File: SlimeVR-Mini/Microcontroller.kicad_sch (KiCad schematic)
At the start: 8 parts, among them U1 ESP32-C3-MINI-1-N4

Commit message: IMU wiring done-ish
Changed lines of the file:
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@@
     (effects (font (size 1.27 1.27)) (justify left bottom))
+  )
+  (hierarchical_label "SDA" (shape input) (at 181.61 105.41 0) (fields_autoplaced)
+    (effects (font (size 1.27 1.27)) (justify left))
+  )
+  (hierarchical_label "SCL" (shape input) (at 181.61 107.95 0) (fields_autoplaced)
+    (effects (font (size 1.27 1.27)) (justify left))
   )
   (symbol (lib_id "power:GND") (at 106.68 111.76 0) (unit 1)

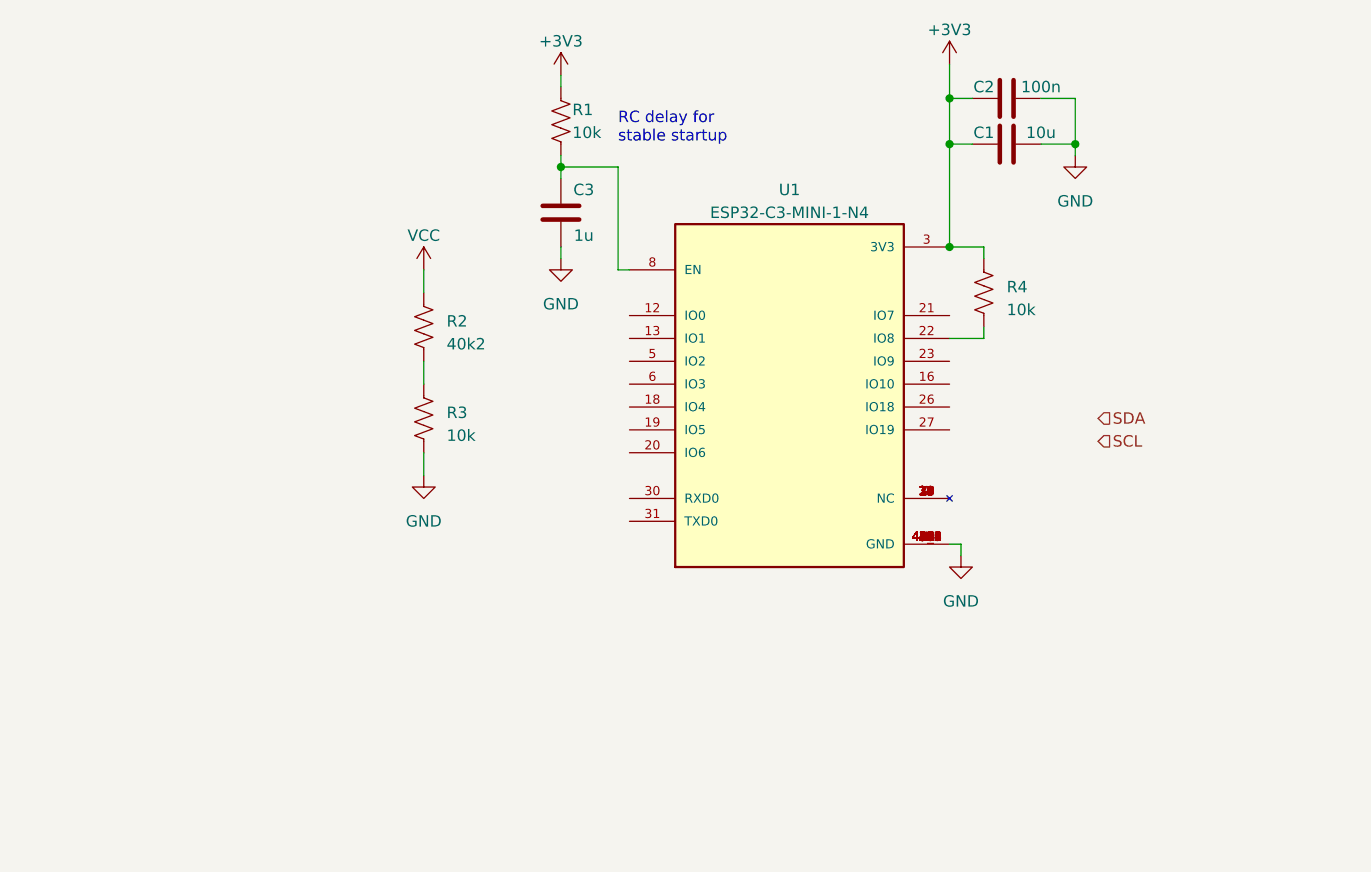
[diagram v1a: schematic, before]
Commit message: added Power page + fixing symbols and footprints
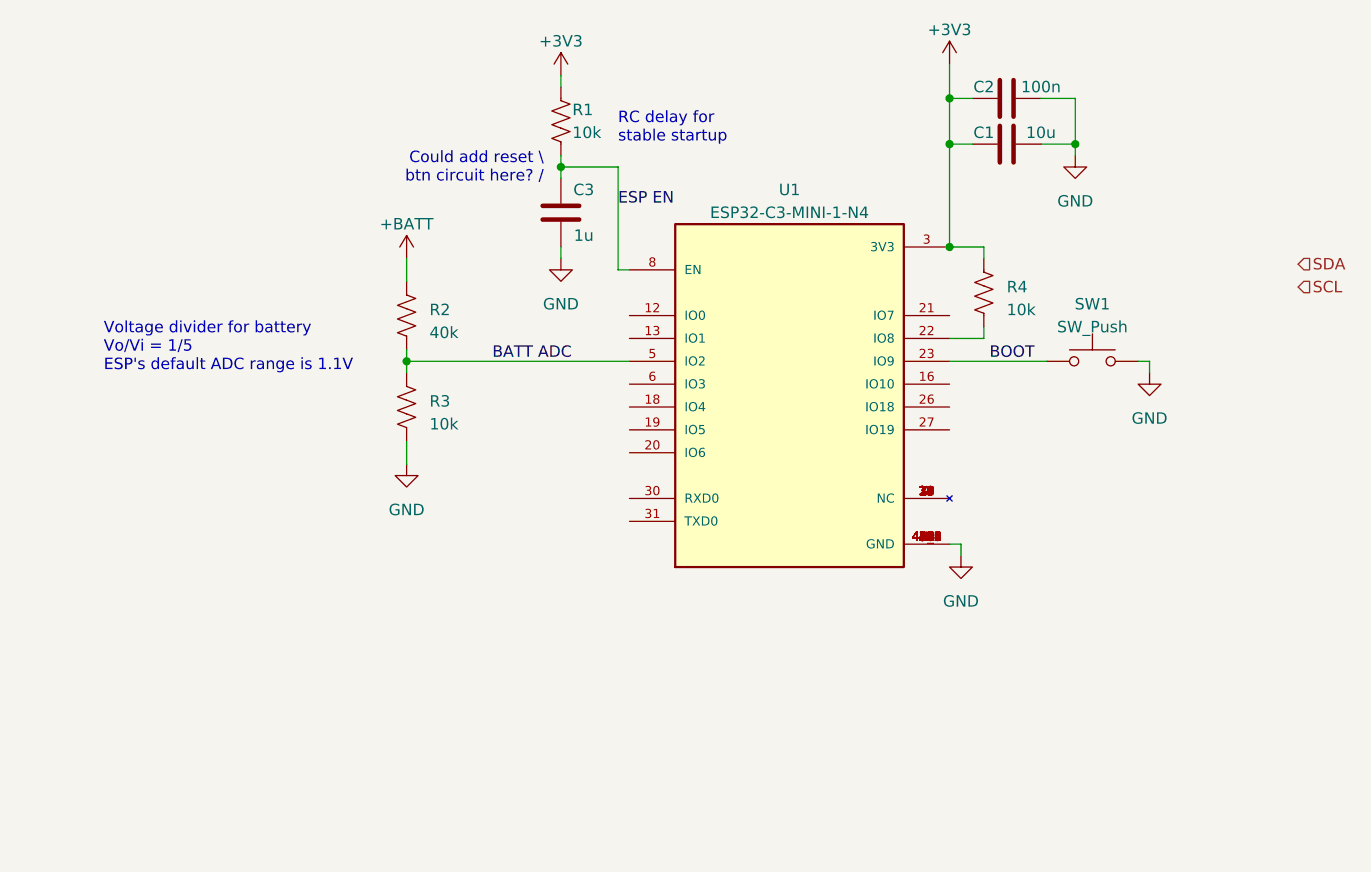
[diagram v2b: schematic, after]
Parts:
- added SW1: SW_Push, symbol Switch:SW_Push
- R2: value 40k2 -> 40k
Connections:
- net GND: now also SW1.2
- net ESP EN: now reaches C3.1, R1.2, U1.8 (EN)
- net BOOT: now reaches U1.23 (IO9)
- net BOOT: now also SW1.1
- net BATT ADC: now reaches U1.5 (IO2)
- net BATT ADC: now also R2.2, R3.1
- net VCC renamed +BATT
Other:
- note added: "Could add reset \ btn circuit here? /"
- note added: "Voltage divider for battery Vo/Vi = 1/5 ESP's default ADC range is 1.1V"
- moved on the sheet: R2, R3
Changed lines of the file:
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@@
   (junction (at 165.1 86.36) (diameter 0) (color 0 0 0 0)
   )
+  (junction (at 104.775 99.06) (diameter 0) (color 0 0 0 0)
+  )
   (junction (at 165.1 69.85) (diameter 0) (color 0 0 0 0)
   )
@@
     (stroke (width 0) (type default))
   )
+  (wire (pts (xy 104.775 99.06) (xy 104.775 100.33))
+    (stroke (width 0) (type default))
+  )
+  (wire (pts (xy 187.325 99.06) (xy 187.325 100.33))
+    (stroke (width 0) (type default))
+  )
   (wire (pts (xy 179.07 69.85) (xy 179.07 74.93))
     (stroke (width 0) (type default))
@@
     (stroke (width 0) (type default))
   )
-  (wire (pts (xy 106.68 88.9) (xy 106.68 91.44))
-    (stroke (width 0) (type default))
-  )
-  (wire (pts (xy 106.68 99.06) (xy 106.68 101.6))
+  (wire (pts (xy 104.775 87.63) (xy 104.775 90.17))
+    (stroke (width 0) (type default))
+  )
+  (wire (pts (xy 104.775 97.79) (xy 104.775 99.06))
     (stroke (width 0) (type default))
   )
@@
     (stroke (width 0) (type default))
   )
-  (wire (pts (xy 106.68 109.22) (xy 106.68 111.76))
+  (wire (pts (xy 104.775 107.95) (xy 104.775 110.49))
+    (stroke (width 0) (type default))
+  )
+  (wire (pts (xy 186.055 99.06) (xy 187.325 99.06))
     (stroke (width 0) (type default))
   )
@@
     (stroke (width 0) (type default))
   )
+  (wire (pts (xy 104.775 99.06) (xy 129.54 99.06))
+    (stroke (width 0) (type default))
+  )
   (wire (pts (xy 165.1 119.38) (xy 166.37 119.38))
     (stroke (width 0) (type default))
   )
+  (wire (pts (xy 165.1 99.06) (xy 175.895 99.06))
+    (stroke (width 0) (type default))
+  )
   (wire (pts (xy 165.1 66.04) (xy 165.1 69.85))
     (stroke (width 0) (type default))
@@
   (wire (pts (xy 121.92 67.31) (xy 121.92 68.58))
     (stroke (width 0) (type default))
+  )
+  (text "Voltage divider for battery\nVo/Vi = 1/5\nESP's default ADC range is 1.1V"
+    (at 71.12 100.33 0)
+    (effects (font (size 1.27 1.27)) (justify left bottom))
   )
   (text "RC delay for\nstable startup" (at 128.27 74.93 0)
     (effects (font (size 1.27 1.27)) (justify left bottom))
   )
-  (hierarchical_label "SDA" (shape input) (at 181.61 105.41 0) (fields_autoplaced)
+  (text "Could add reset \\\nbtn circuit here? /" (at 120.015 79.375 0)
+    (effects (font (size 1.27 1.27)) (justify right bottom))
+  )
+  (label "BOOT" (at 169.545 99.06 0) (fields_autoplaced)
+    (effects (font (size 1.27 1.27)) (justify left bottom))
+  )
+  (label "BATT ADC" (at 114.3 99.06 0) (fields_autoplaced)
+    (effects (font (size 1.27 1.27)) (justify left bottom))
+  )
+  (label "ESP EN" (at 128.27 81.915 0) (fields_autoplaced)
+    (effects (font (size 1.27 1.27)) (justify left bottom))
+  )
+  (hierarchical_label "SDA" (shape input) (at 203.835 88.265 0) (fields_autoplaced)
     (effects (font (size 1.27 1.27)) (justify left))
   )
-  (hierarchical_label "SCL" (shape input) (at 181.61 107.95 0) (fields_autoplaced)
+  (hierarchical_label "SCL" (shape input) (at 203.835 90.805 0) (fields_autoplaced)
     (effects (font (size 1.27 1.27)) (justify left))
   )
-  (symbol (lib_id "power:GND") (at 106.68 111.76 0) (unit 1)
-    (in_bom yes) (on_board yes) (dnp no) (fields_autoplaced)
-    (property "Reference" "#PWR03" (at 106.68 118.11 0)
-      (effects (font (size 1.27 1.27)) hide)
-    )
-    (property "Value" "GND" (at 106.68 116.84 0)
-      (effects (font (size 1.27 1.27)))
-    )
-    (property "Footprint" "" (at 106.68 111.76 0)
-      (effects (font (size 1.27 1.27)) hide)
-    )
-    (property "Datasheet" "" (at 106.68 111.76 0)
+  (symbol (lib_id "power:GND") (at 187.325 100.33 0) (unit 1)
+    (in_bom yes) (on_board yes) (dnp no) (fields_autoplaced)
+    (property "Reference" "#PWR04" (at 187.325 106.68 0)
+      (effects (font (size 1.27 1.27)) hide)
+    )
+    (property "Value" "GND" (at 187.325 105.41 0)
+      (effects (font (size 1.27 1.27)))
+    )
+    (property "Footprint" "" (at 187.325 100.33 0)
+      (effects (font (size 1.27 1.27)) hide)
+    )
+    (property "Datasheet" "" (at 187.325 100.33 0)
+      (effects (font (size 1.27 1.27)) hide)
+    )
+    (pin "1")
+    (instances
+      (project "SlimeVR-Mini"
+        (path "/01f70e2f-47c6-495b-b6f7-eee456c9fb57"
+          (reference "#PWR04") (unit 1)
+        )
+        (path "/01f70e2f-47c6-495b-b6f7-eee456c9fb57/35e02d93-cdac-48f7-b47e-4a5ff7382a35"
+          (reference "#PWR012") (unit 1)
+        )
+      )
+    )
+  )
+  (symbol (lib_id "power:GND") (at 104.775 110.49 0) (unit 1)
+    (in_bom yes) (on_board yes) (dnp no) (fields_autoplaced)
+    (property "Reference" "#PWR03" (at 104.775 116.84 0)
+      (effects (font (size 1.27 1.27)) hide)
+    )
+    (property "Value" "GND" (at 104.775 115.57 0)
+      (effects (font (size 1.27 1.27)))
+    )
+    (property "Footprint" "" (at 104.775 110.49 0)
+      (effects (font (size 1.27 1.27)) hide)
+    )
+    (property "Datasheet" "" (at 104.775 110.49 0)
       (effects (font (size 1.27 1.27)) hide)
     )
@@
         (path "/01f70e2f-47c6-495b-b6f7-eee456c9fb57/35e02d93-cdac-48f7-b47e-4a5ff7382a35"
           (reference "#PWR03") (unit 1)
+        )
+      )
+    )
+  )
+  (symbol (lib_id "power:+BATT") (at 104.775 87.63 0) (unit 1)
+    (in_bom yes) (on_board yes) (dnp no) (fields_autoplaced)
+    (property "Reference" "#PWR011" (at 104.775 91.44 0)
+      (effects (font (size 1.27 1.27)) hide)
+    )
+    (property "Value" "+BATT" (at 104.775 83.82 0)
+      (effects (font (size 1.27 1.27)))
+    )
+    (property "Footprint" "" (at 104.775 87.63 0)
+      (effects (font (size 1.27 1.27)) hide)
+    )
+    (property "Datasheet" "" (at 104.775 87.63 0)
+      (effects (font (size 1.27 1.27)) hide)
+    )
+    (pin "1")
+    (instances
+      (project "SlimeVR-Mini"
+        (path "/01f70e2f-47c6-495b-b6f7-eee456c9fb57/35e02d93-cdac-48f7-b47e-4a5ff7382a35"
+          (reference "#PWR011") (unit 1)
         )
       )
@@
     )
   )
-  (symbol (lib_id "Device:R_US") (at 106.68 95.25 0) (unit 1)
-    (in_bom yes) (on_board yes) (dnp no) (fields_autoplaced)
-    (property "Reference" "R2" (at 109.22 94.615 0)
-      (effects (font (size 1.27 1.27)) (justify left))
-    )
-    (property "Value" "40k2" (at 109.22 97.155 0)
-      (effects (font (size 1.27 1.27)) (justify left))
-    )
-    (property "Footprint" "" (at 107.696 95.504 90)
-      (effects (font (size 1.27 1.27)) hide)
-    )
-    (property "Datasheet" "~" (at 106.68 95.25 0)
+  (symbol (lib_id "Device:R_US") (at 104.775 93.98 0) (unit 1)
+    (in_bom yes) (on_board yes) (dnp no) (fields_autoplaced)
+    (property "Reference" "R2" (at 107.315 93.345 0)
+      (effects (font (size 1.27 1.27)) (justify left))
+    )
+    (property "Value" "40k" (at 107.315 95.885 0)
+      (effects (font (size 1.27 1.27)) (justify left))
+    )
+    (property "Footprint" "" (at 105.791 94.234 90)
+      (effects (font (size 1.27 1.27)) hide)
+    )
+    (property "Datasheet" "~" (at 104.775 93.98 0)
       (effects (font (size 1.27 1.27)) hide)
     )
@@
     )
   )
-  (symbol (lib_id "Device:R_US") (at 106.68 105.41 0) (unit 1)
-    (in_bom yes) (on_board yes) (dnp no) (fields_autoplaced)
-    (property "Reference" "R3" (at 109.22 104.775 0)
-      (effects (font (size 1.27 1.27)) (justify left))
-    )
-    (property "Value" "10k" (at 109.22 107.315 0)
-      (effects (font (size 1.27 1.27)) (justify left))
-    )
-    (property "Footprint" "" (at 107.696 105.664 90)
-      (effects (font (size 1.27 1.27)) hide)
-    )
-    (property "Datasheet" "~" (at 106.68 105.41 0)
+  (symbol (lib_id "Device:R_US") (at 104.775 104.14 0) (unit 1)
+    (in_bom yes) (on_board yes) (dnp no) (fields_autoplaced)
+    (property "Reference" "R3" (at 107.315 103.505 0)
+      (effects (font (size 1.27 1.27)) (justify left))
+    )
+    (property "Value" "10k" (at 107.315 106.045 0)
+      (effects (font (size 1.27 1.27)) (justify left))
+    )
+    (property "Footprint" "" (at 105.791 104.394 90)
+      (effects (font (size 1.27 1.27)) hide)
+    )
+    (property "Datasheet" "~" (at 104.775 104.14 0)
       (effects (font (size 1.27 1.27)) hide)
     )
@@
     )
   )
-  (symbol (lib_id "power:VCC") (at 106.68 88.9 0) (unit 1)
-    (in_bom yes) (on_board yes) (dnp no) (fields_autoplaced)
-    (property "Reference" "#PWR02" (at 106.68 92.71 0)
-      (effects (font (size 1.27 1.27)) hide)
-    )
-    (property "Value" "VCC" (at 106.68 85.09 0)
-      (effects (font (size 1.27 1.27)))
-    )
-    (property "Footprint" "" (at 106.68 88.9 0)
-      (effects (font (size 1.27 1.27)) hide)
-    )
-    (property "Datasheet" "" (at 106.68 88.9 0)
-      (effects (font (size 1.27 1.27)) hide)
-    )
-    (pin "1")
-    (instances
-      (project "SlimeVR-Mini"
-        (path "/01f70e2f-47c6-495b-b6f7-eee456c9fb57"
-          (reference "#PWR02") (unit 1)
-        )
-        (path "/01f70e2f-47c6-495b-b6f7-eee456c9fb57/35e02d93-cdac-48f7-b47e-4a5ff7382a35"
-          (reference "#PWR02") (unit 1)
-        )
-      )
-    )
-  )
   (symbol (lib_id "Device:C") (at 171.45 69.85 270) (unit 1)
     (in_bom yes) (on_board yes) (dnp no)
@@
         )
       )
+    )
+  )
+  (symbol (lib_id "Switch:SW_Push") (at 180.975 99.06 0) (unit 1)
+    (in_bom yes) (on_board yes) (dnp no) (fields_autoplaced)
+    (property "Reference" "SW1" (at 180.975 92.71 0)
+      (effects (font (size 1.27 1.27)))
+    )
+    (property "Value" "SW_Push" (at 180.975 95.25 0)
+      (effects (font (size 1.27 1.27)))
+    )
+    (property "Footprint" "" (at 180.975 93.98 0)
+      (effects (font (size 1.27 1.27)) hide)
+    )
+    (property "Datasheet" "~" (at 180.975 93.98 0)
+      (effects (font (size 1.27 1.27)) hide)
+    )
+    (pin "1")
+    (pin "2")
+    (instances
+      (project "SlimeVR-Mini"
+        (path "/01f70e2f-47c6-495b-b6f7-eee456c9fb57/35e02d93-cdac-48f7-b47e-4a5ff7382a35"
+          (reference "SW1") (unit 1)
+        )
+      )

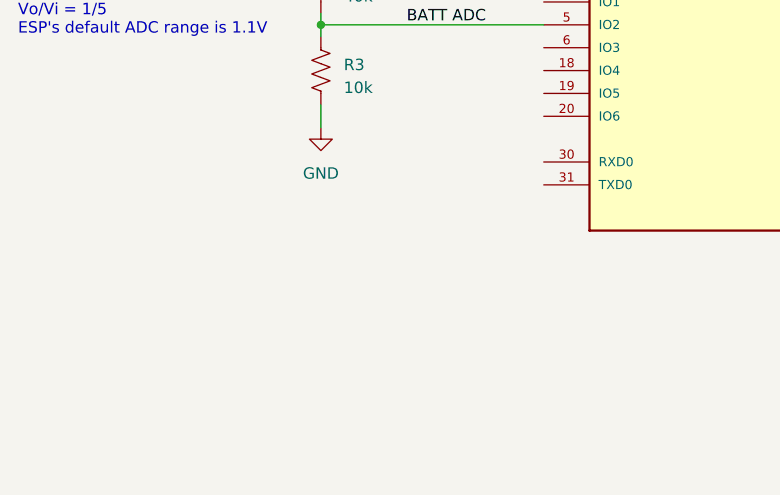
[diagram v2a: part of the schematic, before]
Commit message: added CH340N + schematics development
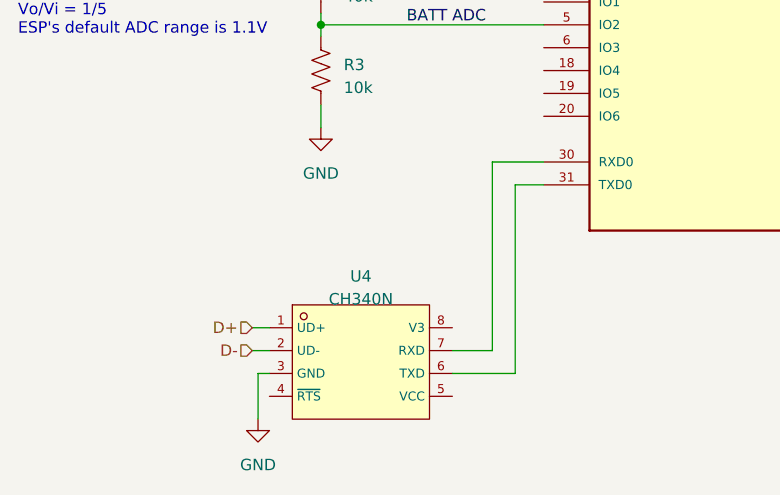
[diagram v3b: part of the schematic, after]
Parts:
- added U4: CH340N, easyeda2kicad:SOP-8_L4.9-W3.9-P1.27-LS6.0-BL, symbol Project Library:CH340N
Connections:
- net GND: now also U4.3 (GND)
- net at U1.30 (RXD0): now also U4.7 (RXD)
- net at U1.31 (TXD0): now also U4.6 (TXD)
- new net D+: U4.1 (UD+)
- new net D-: U4.2 (UD-)
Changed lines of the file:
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@@
+    (stroke (width 0) (type default))
+  )
+  (wire (pts (xy 123.825 135.255) (xy 123.825 114.3))
     (stroke (width 0) (type default))
   )
@@
     (stroke (width 0) (type default))
   )
+  (wire (pts (xy 123.825 114.3) (xy 129.54 114.3))
+    (stroke (width 0) (type default))
+  )
+  (wire (pts (xy 126.365 116.84) (xy 126.365 137.795))
+    (stroke (width 0) (type default))
+  )
   (wire (pts (xy 179.07 74.93) (xy 179.07 76.2))
     (stroke (width 0) (type default))
@@
     (stroke (width 0) (type default))
   )
+  (wire (pts (xy 97.79 137.795) (xy 97.79 142.875))
+    (stroke (width 0) (type default))
+  )
   (wire (pts (xy 121.92 77.47) (xy 128.27 77.47))
     (stroke (width 0) (type default))
@@
     (stroke (width 0) (type default))
   )
+  (wire (pts (xy 119.38 135.255) (xy 123.825 135.255))
+    (stroke (width 0) (type default))
+  )
+  (wire (pts (xy 126.365 137.795) (xy 119.38 137.795))
+    (stroke (width 0) (type default))
+  )
+  (wire (pts (xy 97.155 135.255) (xy 99.06 135.255))
+    (stroke (width 0) (type default))
+  )
   (wire (pts (xy 165.1 74.93) (xy 167.64 74.93))
     (stroke (width 0) (type default))
@@
     (stroke (width 0) (type default))
   )
+  (wire (pts (xy 99.06 137.795) (xy 97.79 137.795))
+    (stroke (width 0) (type default))
+  )
   (wire (pts (xy 128.27 88.9) (xy 129.54 88.9))
     (stroke (width 0) (type default))
@@
   )
   (wire (pts (xy 165.1 74.93) (xy 165.1 86.36))
+    (stroke (width 0) (type default))
+  )
+  (wire (pts (xy 129.54 116.84) (xy 126.365 116.84))
+    (stroke (width 0) (type default))
+  )
+  (wire (pts (xy 97.155 132.715) (xy 99.06 132.715))
     (stroke (width 0) (type default))
   )
@@
     (effects (font (size 1.27 1.27)) (justify left))
   )
+  (hierarchical_label "D+" (shape input) (at 97.155 132.715 180) (fields_autoplaced)
+    (effects (font (size 1.27 1.27)) (justify right))
+  )
   (hierarchical_label "SCL" (shape input) (at 203.835 90.805 0) (fields_autoplaced)
     (effects (font (size 1.27 1.27)) (justify left))
+  )
+  (hierarchical_label "D-" (shape input) (at 97.155 135.255 180) (fields_autoplaced)
+    (effects (font (size 1.27 1.27)) (justify right))
   )
   (symbol (lib_id "power:GND") (at 187.325 100.33 0) (unit 1)
@@
     )
   )
+  (symbol (lib_id "Project Library:CH340N") (at 109.22 137.795 0) (unit 1)
+    (in_bom yes) (on_board yes) (dnp no) (fields_autoplaced)
+    (property "Reference" "U4" (at 109.22 127 0)
+      (effects (font (size 1.27 1.27)))
+    )
+    (property "Value" "CH340N" (at 109.22 129.54 0)
+      (effects (font (size 1.27 1.27)))
+    )
+    (property "Footprint" "easyeda2kicad:SOP-8_L4.9-W3.9-P1.27-LS6.0-BL" (at 109.22 147.955 0)
+      (effects (font (size 1.27 1.27)) hide)
+    )
+    (property "Datasheet" "" (at 109.22 137.795 0)
+      (effects (font (size 1.27 1.27)) hide)
+    )
+    (property "LCSC Part" "C2977777" (at 109.22 150.495 0)
+      (effects (font (size 1.27 1.27)) hide)
+    )
+    (pin "1")
+    (pin "2")
+    (pin "3")
+    (pin "4")
+    (pin "5")
+    (pin "6")
+    (pin "7")
+    (pin "8")
+    (instances
+      (project "SlimeVR-Mini"
+        (path "/01f70e2f-47c6-495b-b6f7-eee456c9fb57/35e02d93-cdac-48f7-b47e-4a5ff7382a35"
+          (reference "U4") (unit 1)
+        )
+      )
+    )
+  )
   (symbol (lib_id "Device:R_US") (at 168.91 91.44 0) (unit 1)
     (in_bom yes) (on_board yes) (dnp no) (fields_autoplaced)
@@
         )
       )
+    )
+  )
+  (symbol (lib_id "power:GND") (at 97.79 142.875 0) (unit 1)
+    (in_bom yes) (on_board yes) (dnp no) (fields_autoplaced)
+    (property "Reference" "#PWR03" (at 97.79 149.225 0)
+      (effects (font (size 1.27 1.27)) hide)
+    )
+    (property "Value" "GND" (at 97.79 147.955 0)
+      (effects (font (size 1.27 1.27)))
+    )
+    (property "Footprint" "" (at 97.79 142.875 0)
+      (effects (font (size 1.27 1.27)) hide)
+    )
+    (property "Datasheet" "" (at 97.79 142.875 0)
+      (effects (font (size 1.27 1.27)) hide)
+    )
+    (pin "1")
+    (instances
+      (project "SlimeVR-Mini"
+        (path "/01f70e2f-47c6-495b-b6f7-eee456c9fb57"
+          (reference "#PWR03") (unit 1)
+        )
+        (path "/01f70e2f-47c6-495b-b6f7-eee456c9fb57/35e02d93-cdac-48f7-b47e-4a5ff7382a35"
+          (reference "#PWR015") (unit 1)
+        )
+      )
